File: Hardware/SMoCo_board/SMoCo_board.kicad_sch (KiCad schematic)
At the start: 46 parts, among them J1 Conn_01x02, J2 Conn_01x02, J4 Conn_01x02, J5 Conn_01x06, J6 Conn_01x02, J7 Conn_01x04, J8 Conn_01x02, U1 STM32F072C8T6, U2 VNH7040AYTR, U3 SN65HVD232, U4 AP63203WU

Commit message: SMoC0
Edit after review 1
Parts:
- removed D2, D3, D6: LED, symbol Device:LED
- removed R13, R14, R3: 1k, symbol Device:R_US
- added D1: GREEN, symbol Device:LED
- added R1: 1k, symbol Device:R_US
- C5, C8: value C -> 22uF
- D4: value LED -> GREEN
- H1: footprint SX1262IMLTRT:QFN50P400X400X100-25N -> (none)
- L1: value L -> 3.9 uH
- gave numbers to parts that had none: 1
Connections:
- net ENC_A is gone; now on net ENC A: U1.30 (PA9)
- net LIM2 A is gone; now on net LIM A: U1.39 (PB3)
- net LIM2 B is gone; now on net LIM B: U1.40 (PB4)
- net ENC A: no longer U1.18 (PB0)
- net ENC B: now also U1.29 (PA8); no longer U1.19 (PB1)
- net ENC I: no longer U1.20 (PB2)
- net GND: now also D1.1 (K)
- net LIM A: no longer U1.42 (PB6)
- net LIM B: no longer U1.43 (PB7)
- net at D4.2 (A): now also R10.2
- net at R11.2: now also D1.2 (A)
- net ABS: no longer names the net of U1.38 (PA15)
- net ENC_B: no longer names the net of U1.31 (PA10)
- net IN_A IN renamed IN_A
- net IN_A OUT: no longer names the net of R2.2, U1.10 (PA0)
- net IN_B IN renamed IN_B
- net IN_B: now also R1.1
- net IN_B OUT: no longer names the net of U1.11 (PA1)
- net IN_B OUT: now also R1.2
- net MS IN: no longer names the net of R7.2, R9.1, U1.15 (PA5)
- net MS OUT renamed MS
- net MS_EN IN renamed MS_EN
- net MS_EN OUT: no longer names the net of R8.2, U1.14 (PA4)
- net PWM IN renamed PWM
- net PWM OUT: no longer names the net of R4.2, U1.17 (PA7)
- net SEL0 IN renamed SEL0
- net SEL0 OUT: no longer names the net of R5.2, U1.12 (PA2)
- net SEL1 IN renamed SEL1
- net SEL1 OUT: no longer names the net of R6.2, U1.13 (PA3)
- no-connect marks 6 -> 25
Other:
- note added: "CAN TRANSCEIVER"
- note removed: "CAN TRANSCIEVER"
- note removed: "Motor Activity"
- moved on the sheet: LED1, R10, R11, R15, R16, R17

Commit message: SMoCo Update after Review 2
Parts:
- removed J4: Conn_01x02, symbol Connector_Generic:Conn_01x02
- removed R15: 200, symbol Device:R_US
- removed R16: 350, symbol Device:R_US
- removed R17: 1k, symbol Device:R_US
- added C2: C, symbol Device:C
- added D5: D_TVS, Diode_SMD:D_0603_1608Metric_Pad1.05x0.95mm_HandSolder, symbol Device:D_TVS
- added J3: Conn_01x03, Package_LCC:PLCC-84_29.3x29.3mm_P1.27mm, symbol Connector_Generic:Conn_01x03
- added SW1: SW_Push, Button_Switch_SMD:Nidec_Copal_CAS-120A, symbol Switch:SW_Push
- added TP1: TestPoint, symbol Connector:TestPoint
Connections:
- net +3.3V: now also TP1.1
- net GND: now also U1.44 (BOOT0), C2.2, D5.1 (A1), J3.3 (Pin_3), SW1.1
- net LIM A: now also J3.1 (Pin_1)
- net LIM B: now also J3.2 (Pin_2)
- net switch: now reaches U1.7 (NRST)
- net switch: now also C2.1, D5.2 (A2), SW1.2
- net Led_G_Out: now reaches LED1.2
- net Led_R_Out: now reaches LED1.1
- net Led_B_Out: now reaches LED1.3
- no-connect marks 25 -> 23
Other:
- added sheet Untitled Sheet (Mosfet Circuit for RGB LED.kicad_sch)
- note added: "Reset Button"
- moved on the sheet: C3, R1, R2, R4, R5, R6, R7, R8, R9, U1A, U1B

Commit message: Temp Revision SMoCo
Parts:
- removed H1, H2: MountingHole, symbol Mechanical:MountingHole
- removed SW1: SW_Push, Button_Switch_SMD:Nidec_Copal_CAS-120A, symbol Switch:SW_Push
- added C9: C, symbol Device:C
- added D6: D_TVS, Diode_SMD:D_0603_1608Metric_Pad1.05x0.95mm_HandSolder, symbol Device:D_TVS
- added H1, H2: MountingHole_Pad, symbol Mechanical:MountingHole_Pad
- added JP1, JP2: Jumper_2_Open, Package_LCC:PLCC-84_29.3x29.3mm_P1.27mm, symbol Jumper:Jumper_2_Open
- added U5: STM32F072C8Tx, Package_QFP:LQFP-48_7x7mm_P0.5mm, symbol MCU_ST_STM32F0:STM32F072C8Tx
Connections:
- net GND: now also C9.2, D6.1 (A1), H1.1, H2.1, JP1.1 (A), JP2.1 (A); no longer U1.44 (BOOT0)
- net MS: now also U1.15 (PA5), C9.1; no longer C3.1, U2.19 (MultiSense)
- net at R7.2, R9.1: now also U2.19 (MultiSense); no longer U1.15 (PA5)
- net Vaux renamed V_AUX
- net switch renamed NRST
- net NRST: now also JP1.2 (B)
- new net: U5.23 (VSS), U5.35 (VSS), U5.47 (VSS)
- new net boot: C3.1, D6.2 (A2), JP2.2 (B), U1.44 (BOOT0)
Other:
- moved on the sheet: J2, R1, R2, R4, R5, R6, R8, U1A

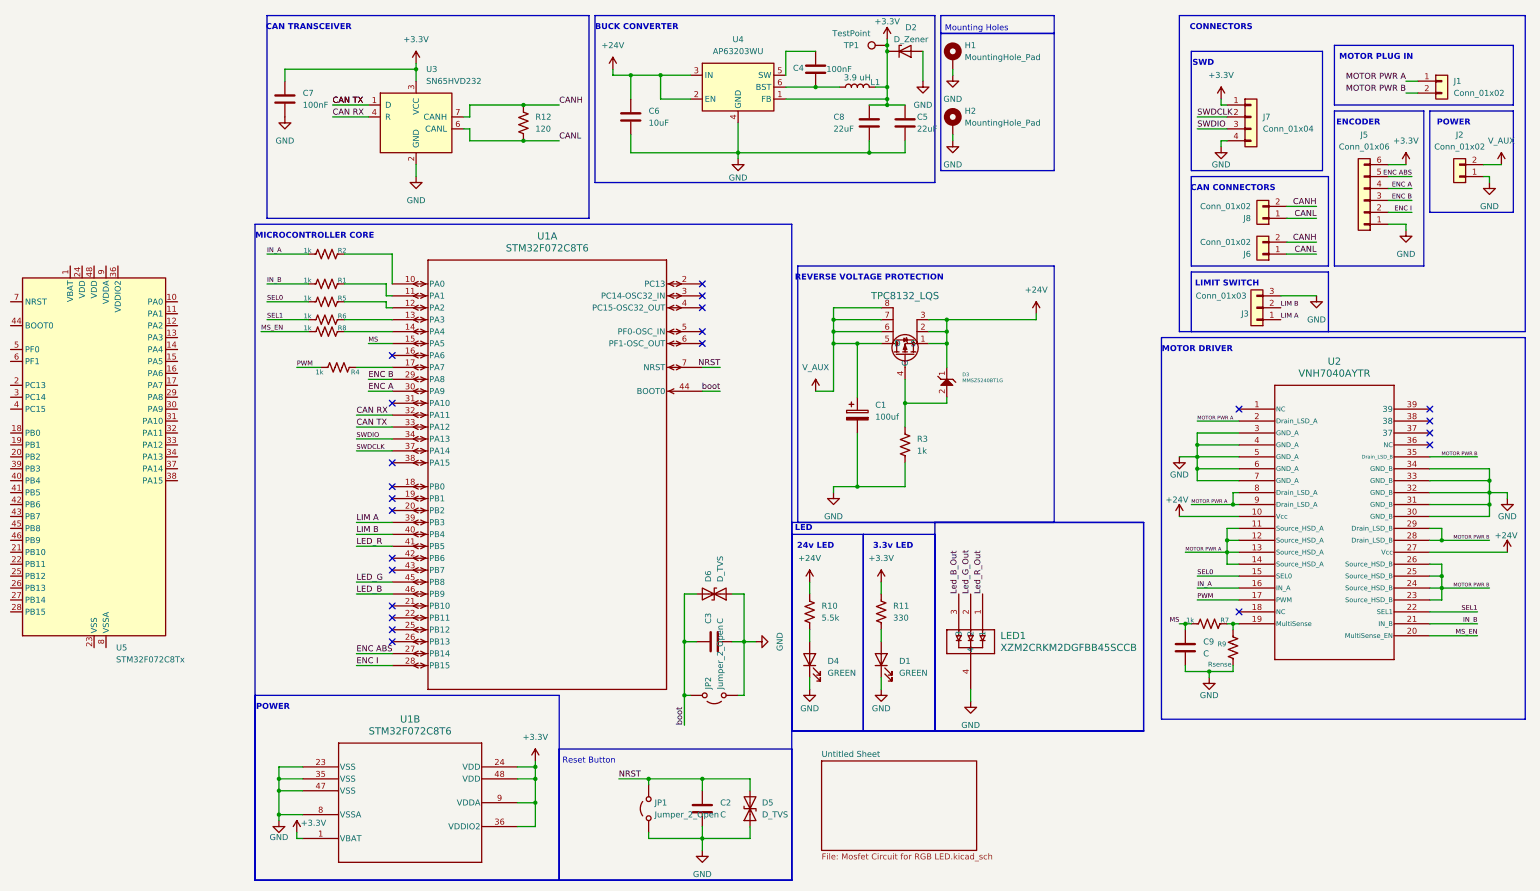
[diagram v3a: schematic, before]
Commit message: Fixed lots of stuff
fixed LED resistor values, bulk capacitor, decoupling capacitors and most data sheets.
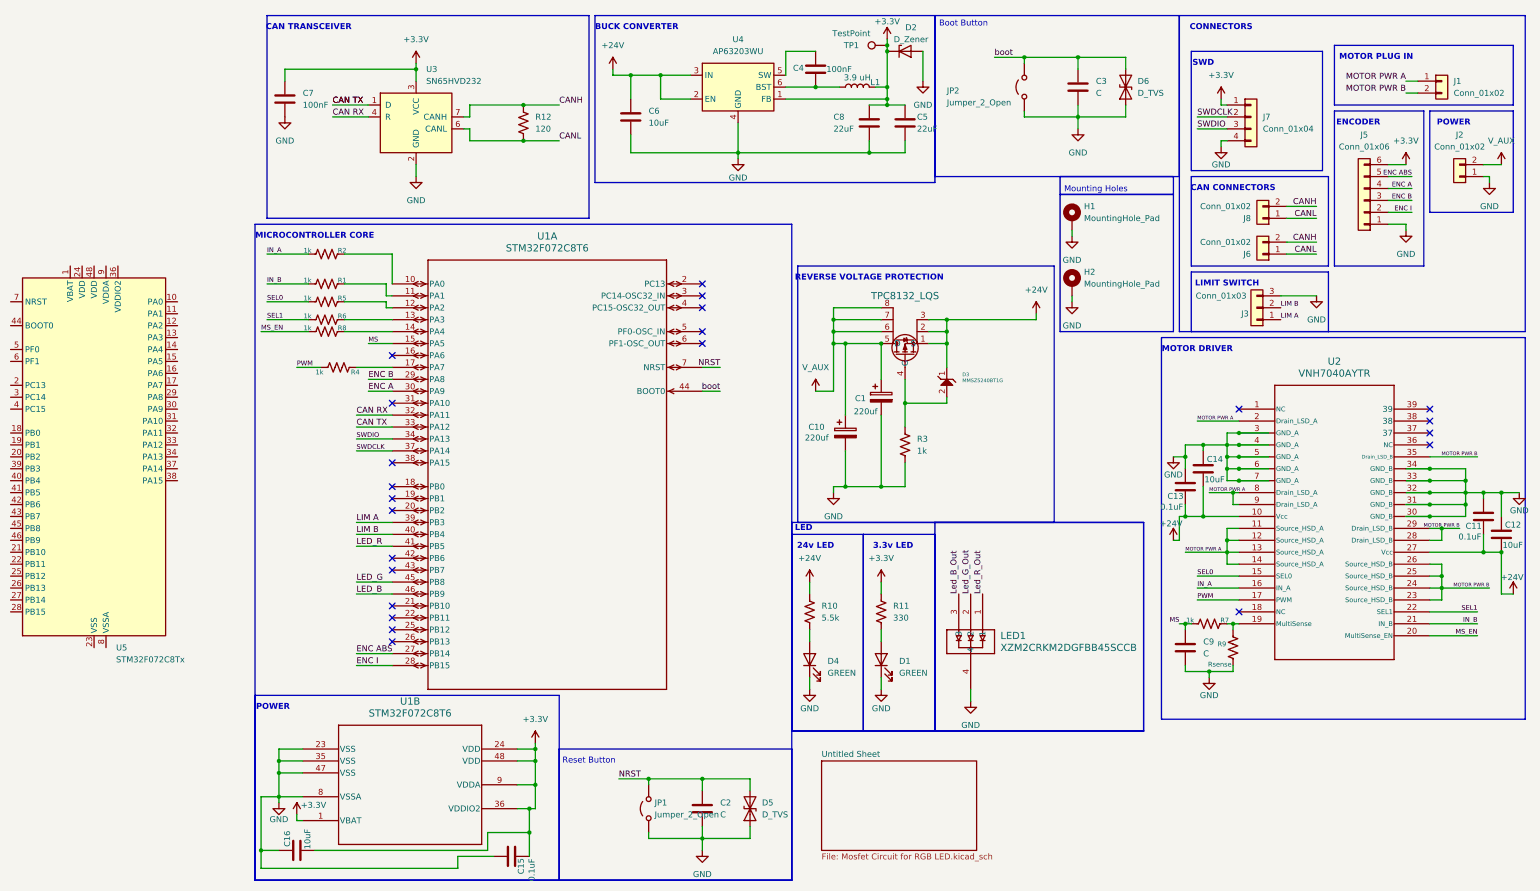
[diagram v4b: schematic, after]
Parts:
- added C10: 220uf, Capacitor_SMD:C_0603_1608Metric_Pad1.08x0.95mm_HandSolder, symbol Device:C_Polarized
- added C11, C13, C15: 0.1uF, symbol Device:C
- added C12, C14, C16: 10uF, symbol Device:C
- C1: value 100uf -> 220uf
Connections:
- net +24V: now also C11.2, C12.2, C13.2, C14.2
- net +3.3V: now also C15.2, C16.2
- net GND: now also C10.2, C11.1, C12.1, C13.1, C14.1, C15.1, C16.1
- net V_AUX: now also C10.1
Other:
- note added: "Boot Button"
- moved on the sheet: C1, H1, H2, U1B

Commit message: Updated with Bulk Capacitor and new STM32 symbol
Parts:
- removed unit 1 of U1
- added C17: 10uF, symbol Device:C
- added C18: 0.1uF, symbol Device:C
- added C19: 47uF, symbol Device:C_Polarized
- C2, C3: value C -> 100nF
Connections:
- net IN_A is gone; now on net GND: R2.1, U2.16 (IN_A)
- net IN_B is gone; now on net +3.3V: R1.1, U2.21 (IN_B)
- net +24V: now also C19.1
- net +3.3V: now also U5.1 (VBAT), U5.24 (VDD), U5.36 (VDDIO2), U5.48 (VDD), U5.9 (VDDA), C17.2, C18.2
- net CAN RX: now also U5.32 (PA11)
- net CAN TX: now also U5.33 (PA12)
- net ENC A: now also U5.30 (PA9)
- net ENC ABS: now also U5.27 (PB14)
- net ENC B: now also U5.29 (PA8)
- net ENC I: now also U5.28 (PB15)
- net GND: now also U5.23 (VSS), U5.35 (VSS), U5.47 (VSS), U5.8 (VSSA), C17.1, C18.1, C19.2
- net LED_B: now also U5.46 (PB9)
- net LED_G: now also U5.45 (PB8)
- net LED_R: now also U5.41 (PB5)
- net LIM A: now also U5.39 (PB3)
- net LIM B: now also U5.40 (PB4)
- net MS: now also U5.15 (PA5)
- net NRST: now also U5.7 (NRST)
- net SWDCLK: now also U5.37 (PA14)
- net SWDIO: now also U5.34 (PA13)
- net boot: now also U5.44 (BOOT0)
- net at R2.2: now also U5.10 (PA0)
- net at R1.2: now also U5.11 (PA1)
- net at R5.2: now also U5.12 (PA2)
- net at R6.2: now also U5.13 (PA3)
- net at R8.2: now also U5.14 (PA4)
- net at R4.2: now also U5.17 (PA7)
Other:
- moved on the sheet: C6, R1, R2, R4, R5, R6, R8, U5

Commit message: SMoCo Schematic Done
Schematic should be done.
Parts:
- removed C15, C18: 0.1uF, symbol Device:C
- removed C16, C17: 10uF, symbol Device:C
- removed U1: STM32F072C8T6, LQFP48-7x7mm, symbol STM32F072C8T6:STM32F072C8T6
- added C20, C24: 4.7uF, symbol Device:C
- added C21, C25, C26, C27: 100nF, symbol Device:C
- added C22: 10nF, symbol Device:C
- added C23: 1uF, symbol Device:C
- C9: value C -> 10nF
- R7: value 1k -> 10k
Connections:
- net +3.3V: now also C20.1, C21.1, C22.1, C23.1, C24.1, C25.1, C26.1, C27.1; no longer R1.1, U2.21 (IN_B)
- net GND: now also C20.2, C21.2, C22.2, C23.2, C24.2, C25.2, C26.2, C27.2; no longer R2.1, U2.16 (IN_A)
- new net IN_A: R2.1, U2.16 (IN_A)
- new net IN_B: R1.1, U2.21 (IN_B)

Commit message: MS Resistor
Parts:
- R9: value Rsense -> 1k

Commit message: Footprints, temp work pcb side
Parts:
- C1, C10: footprint Capacitor_SMD:C_0603_1608Metric_Pad1.08x0.95mm_HandSolder -> Capacitor_THT:CP_Radial_D8.0mm_P3.50mm
- C11, C12, C13, C14, C19, C2, C20, C21, C22, C23, C24, C25, C26, C27, C3, C4, C5, C6, C7, C8, C9: footprint (none) -> Capacitor_SMD:C_0603_1608Metric_Pad1.08x0.95mm_HandSolder
- D1, D4: footprint (none) -> LED_SMD:LED_0603_1608Metric
- D3: footprint MRDT_Devices:SOD-123_ONS-L -> Diode_SMD:D_SOD-123
- H1, H2: footprint (none) -> MountingHole:MountingHole_3.2mm_M3_Pad
- J1, J2: footprint (none) -> Connector_Wire:SolderWire-1.5sqmm_1x02_P6mm_D1.7mm_OD3mm
- J3: footprint Package_LCC:PLCC-84_29.3x29.3mm_P1.27mm -> Connector_Wire:SolderWire-0.5sqmm_1x03_P4.6mm_D0.9mm_OD2.1mm
- J5, J6: footprint (none) -> Connector_Wire:SolderWire-0.5sqmm_1x03_P4.6mm_D0.9mm_OD2.1mm
- J7: footprint (none) -> Connector_PinHeader_2.54mm:PinHeader_1x04_P2.54mm_Vertical
- J8: footprint (none) -> Connector_Wire:SolderWire-0.5sqmm_1x02_P4.6mm_D0.9mm_OD2.1mm
- JP1, JP2: footprint Package_LCC:PLCC-84_29.3x29.3mm_P1.27mm -> Jumper:SolderJumper-2_P1.3mm_Open_Pad1.0x1.5mm
- L1: footprint (none) -> Inductor_SMD:L_Bourns_SRU5016_5.2x5.2mm
- LED1: footprint PLCC4_3p5x2p8_SLD -> footprints:PLCC4_3p5x2p8_SLD
- MOSFET1: footprint MRDT_Devices:SOP-8_TOS-L -> Package_SO:SOIC-8_3.9x4.9mm_P1.27mm
- R1, R10, R11, R12, R2, R4, R5, R6, R7, R8, R9: footprint (none) -> Resistor_SMD:R_0603_1608Metric_Pad0.98x0.95mm_HandSolder
- TP1: footprint (none) -> TestPoint:TestPoint_Pad_D1.5mm
- U2: footprint POWERSSO-36TP_STM -> Package_SO:ST_PowerSSO-36_SlugDown_ThermalVias
